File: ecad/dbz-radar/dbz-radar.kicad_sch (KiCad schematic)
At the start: 139 parts, among them J1 B2B-PH-SM4-TB, J2 USB4220-03-0880-C, J3 XF2M-4015-1A, J4 533980271, J5 DNI, Q1 Q_PMOS, SW1 SKRPACE010, SW2 SKRPACE010, SW3 1-825027-7, U1 USBLC6-2SC6, U2 TPS61169, U3 MCP738311/2, U4 MAX17048/9, U5 AP2112K-3.3, U6 PCA9554, U7 MAX98357A, U8 ESP32-S3-WROOM-1-N16R8

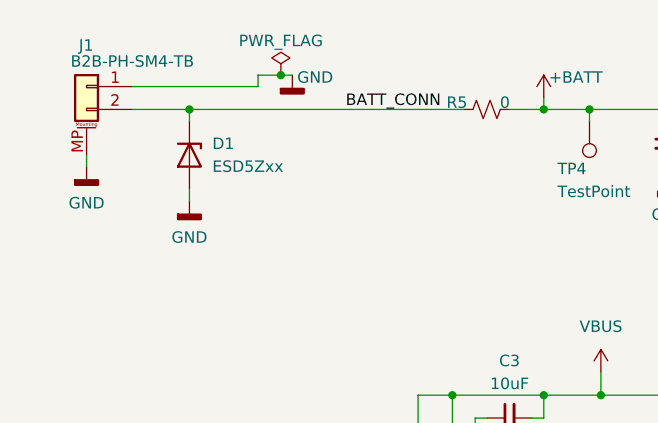
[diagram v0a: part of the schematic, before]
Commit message: flip polarity of battery connector in schematic
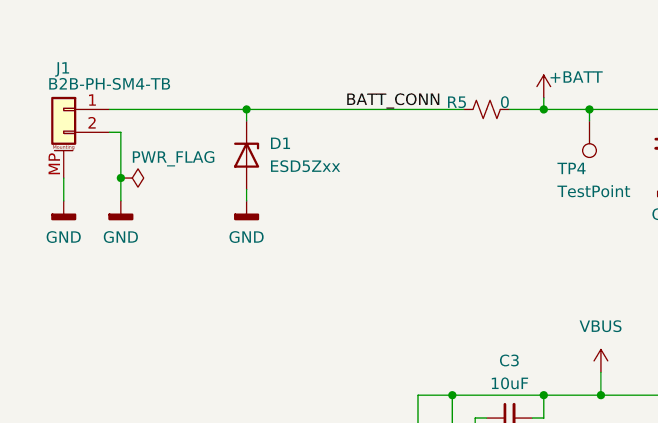
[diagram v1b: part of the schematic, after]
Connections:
- net BATT_CONN: now also J1.1 (Pin_1); no longer J1.2 (Pin_2)
- net GND: now also J1.2 (Pin_2); no longer J1.1 (Pin_1)
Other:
- moved on the sheet: D1, J1

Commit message: fix U4 distributor PN on BOM
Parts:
- U4: LCSC C7497002 -> C2682616
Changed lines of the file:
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@@
 	(title_block
 		(title "Dragon Ball Radar")
-		(date "2026-09-01")
-		(rev "V1.1")
+		(date "2026-08-14")
+		(rev "α2")
 		(company "Extra Long Division")
 		(comment 1 "extralongdivision.com/id/")
@@
 			)
 		)
-		(property "LCSC" "C7497002"
+		(property "LCSC" "C2682616"
 			(at 182.88 27.94 0)
 			(hide yes)
